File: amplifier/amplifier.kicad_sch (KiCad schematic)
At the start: 49 parts, among them J1 GND, J2 IN, J3 +35V, J4 OUT, J5 GND, J6 -35V, Q1 2N5551, Q2 2N5551, Q3 2N5551, Q4 TIP42C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

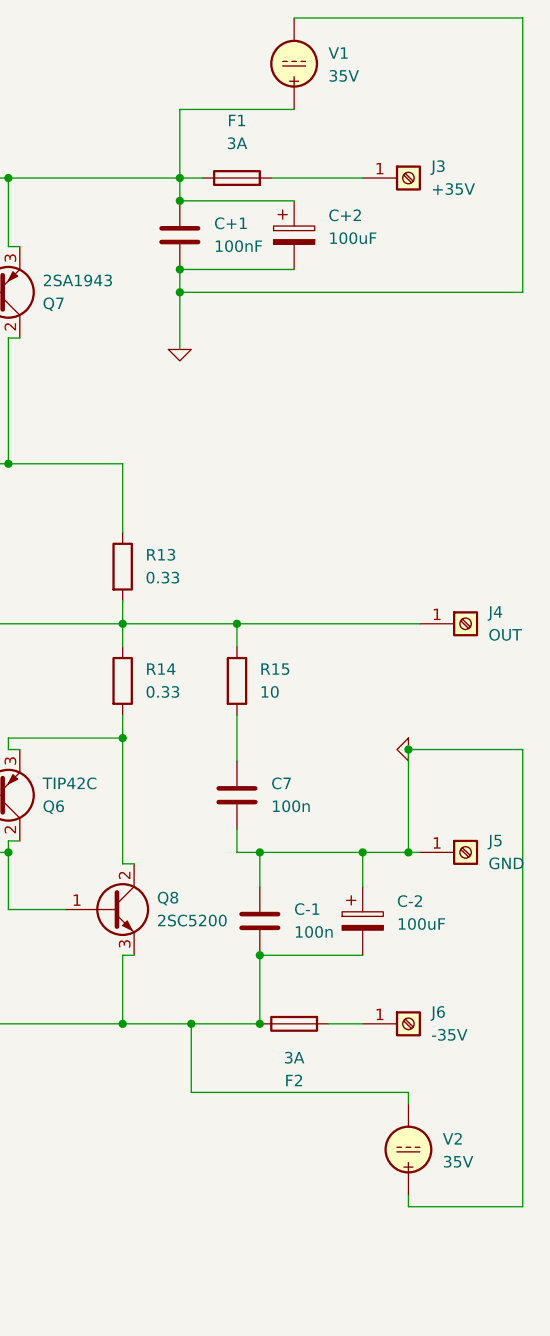
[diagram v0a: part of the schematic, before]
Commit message: 40V upgrade and generate BOM CSVs
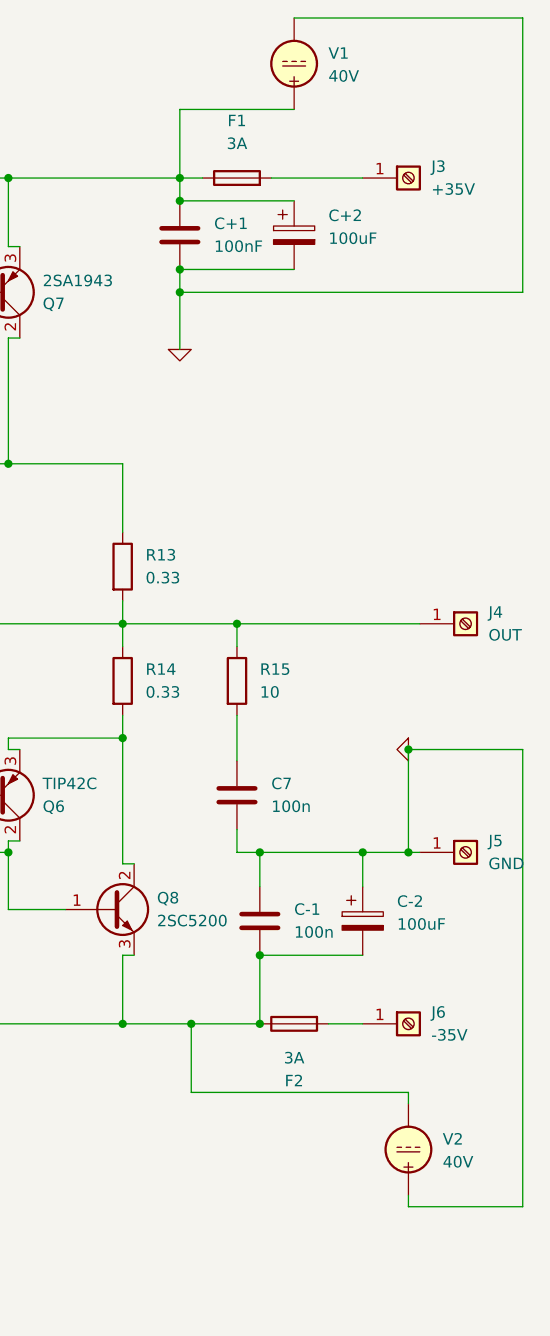
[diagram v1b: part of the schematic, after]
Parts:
- V1, V2: value 35V -> 40V
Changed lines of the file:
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@@
 			)
 		)
-		(property "Value" "35V"
+		(property "Value" "40V"
 			(at 232.41 147.4497 0)
 			(effects
@@
 			)
 		)
-		(property "Value" "35V"
+		(property "Value" "40V"
 			(at 219.71 26.7997 0)
 			(effects
